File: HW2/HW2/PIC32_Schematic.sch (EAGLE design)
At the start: 22 parts

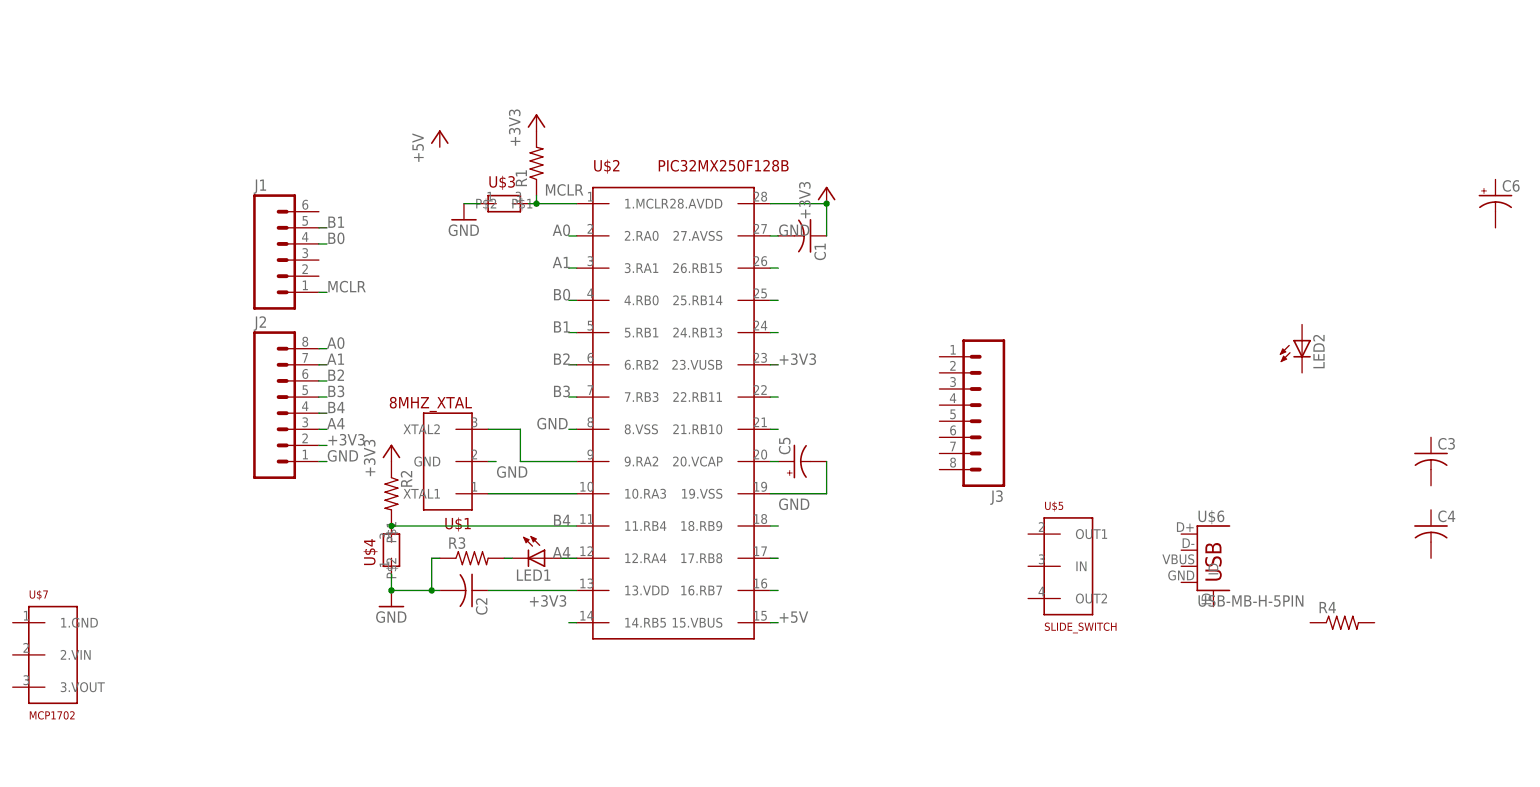
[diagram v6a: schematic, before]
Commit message: All PIC32 pins are now connected
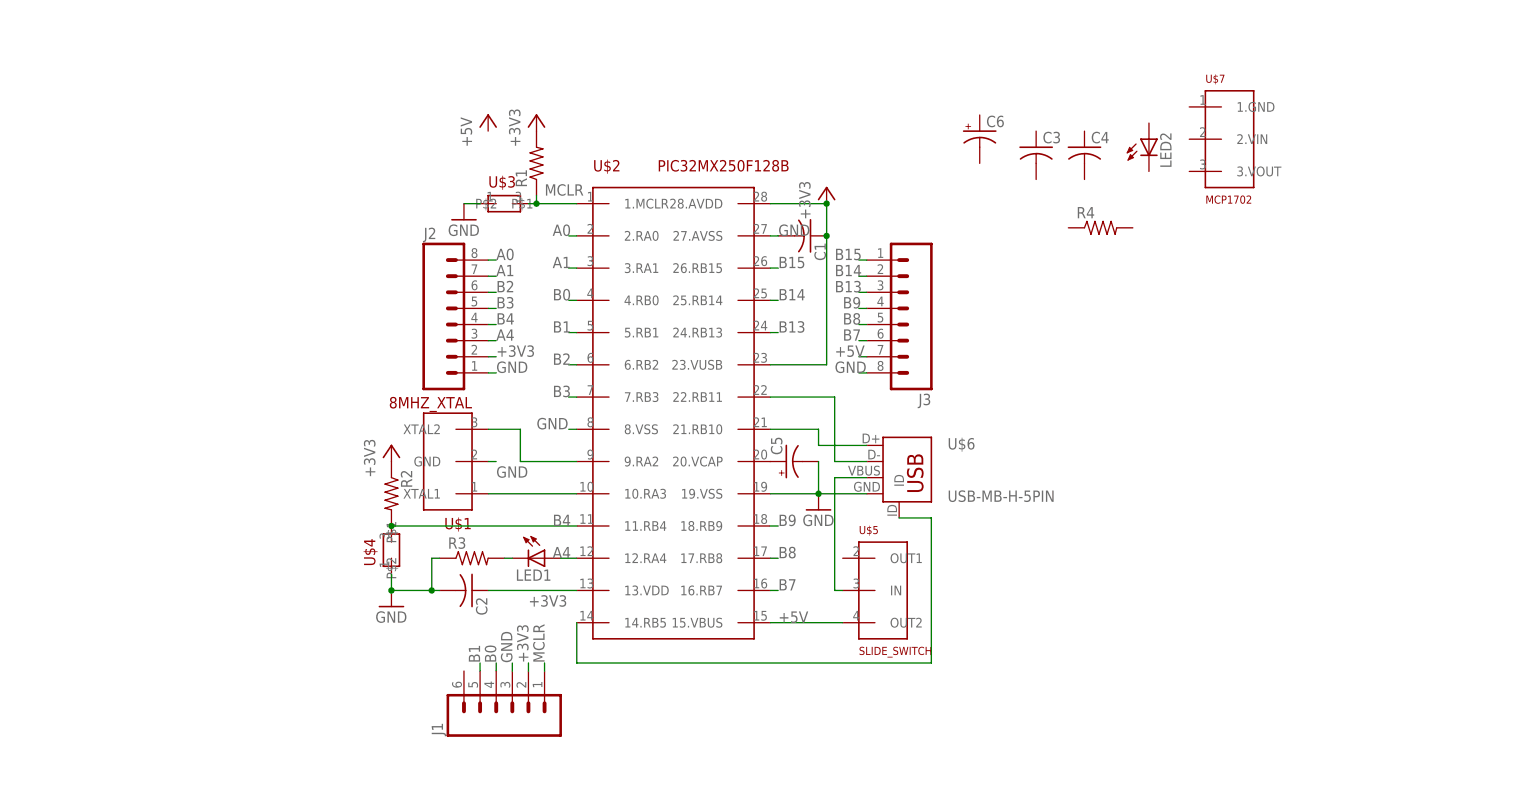
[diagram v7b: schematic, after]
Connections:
- removed net N$11: U$2.18.RB9
- removed net N$12: U$2.17.RB8
- removed net N$13: U$2.16.RB7
- removed net N$15: U$2.14.RB5
- removed net N$3: U$2.26.RB15
- removed net N$4: U$2.25.RB14
- removed net N$5: U$2.24.RB13
- removed net N$7: U$2.22.RB11
- removed net N$8: U$2.21.RB10
- new net B13: J3.3, U$2.24.RB13
- new net B14: J3.2, U$2.25.RB14
- new net B15: J3.1, U$2.26.RB15
- new net B7: J3.6, U$2.16.RB7
- new net B8: J3.5, U$2.17.RB8
- new net B9: J3.4, U$2.18.RB9
- new net D+: U$2.21.RB10, U$6.D+
- new net D-: U$2.22.RB11, U$6.D-
- new net ID: U$2.14.RB5, U$6.ID
- new net N$2: U$5.IN, U$6.VBUS
- net +3V3: now also J1.2
- net +5V: now also J3.7, U$5.OUT2
- net GND: now also J1.3, J3.8, U$6.GND
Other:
- moved on the sheet: C3, C4, C5, C6, J1, J2, J3, LED2, R4, U$5, U$7

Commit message: Schematic is complete; verification needed
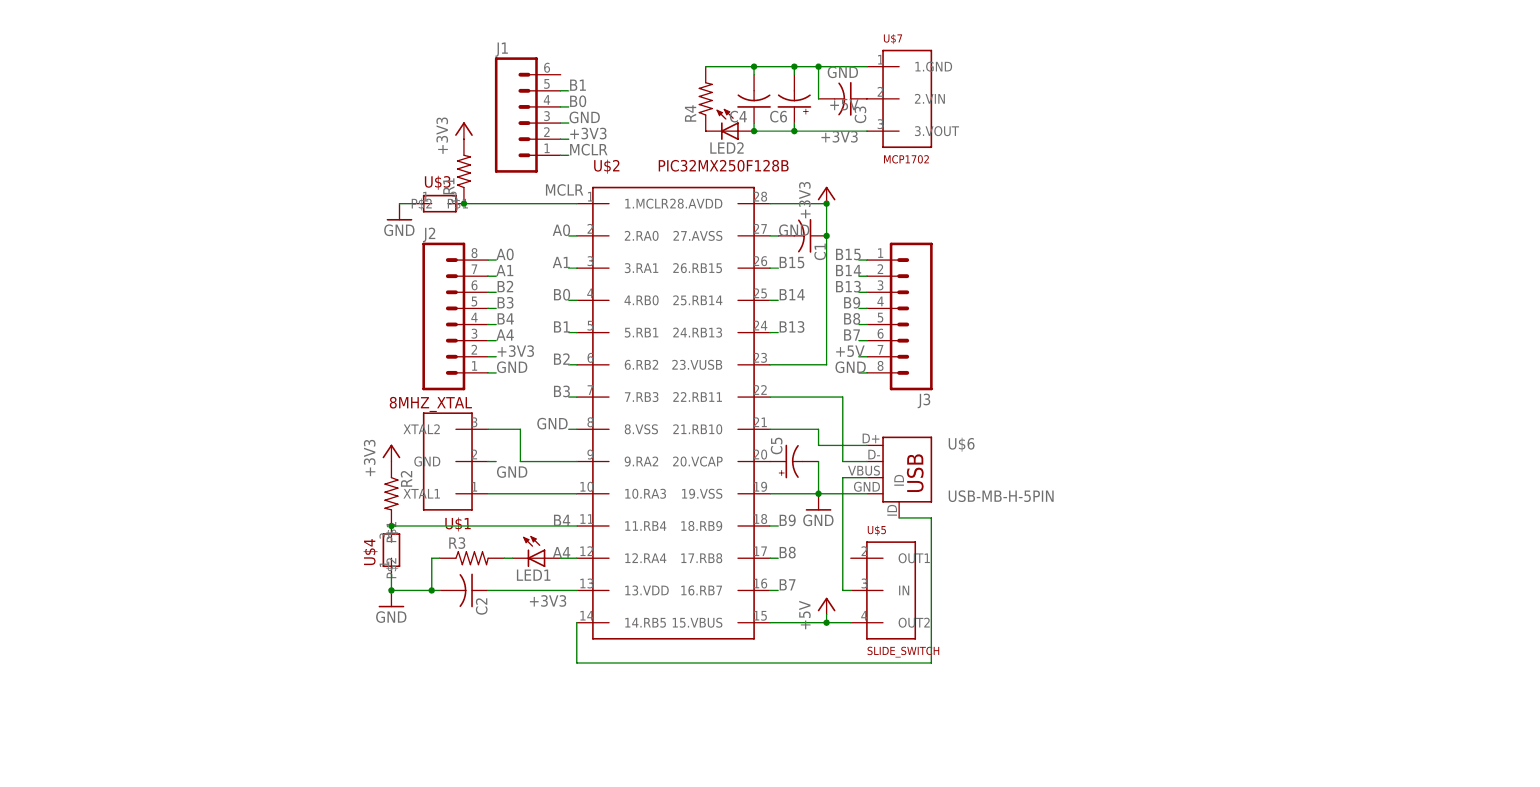
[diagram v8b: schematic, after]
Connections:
- new net N$3: LED2.C, R4.1
- net +3V3: now also C4.1, C6.+, LED2.A, U$7.3.VOUT
- net +5V: now also C3.1, U$7.2.VIN
- net GND: now also C3.2, C4.2, C6.-, R4.2, U$7.1.GND
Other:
- moved on the sheet: C3, C4, C6, J1, LED2, R1, R4, U$3, U$5, U$7
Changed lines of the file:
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@@
 <part name="R2" library="ME433" deviceset="R-US_" device="0207/10"/>
 <part name="R3" library="ME433" deviceset="R-US_" device="0207/10"/>
-<part name="R4" library="ME433" deviceset="R-US_" device="0207/10"/>
 <part name="C1" library="ME433" deviceset="C-US" device="025-024X044"/>
 <part name="C2" library="ME433" deviceset="C-US" device="025-024X044"/>
@@
 <part name="+3V3" library="ME433" deviceset="+3V3" device=""/>
 <part name="GND1" library="ME433" deviceset="GND" device=""/>
+<part name="R4" library="ME433" deviceset="R-US_" device="0207/10"/>
 </parts>
 <sheets>
@@
 <instance part="U$1" gate="G$1" x="-29.21" y="-2.54" rot="R180"/>
 <instance part="U$2" gate="G$1" x="0" y="0"/>
-<instance part="U$3" gate="G$1" x="-26.67" y="33.02"/>
+<instance part="U$3" gate="G$1" x="-36.83" y="33.02"/>
 <instance part="U$4" gate="G$1" x="-44.45" y="-21.59" rot="R90"/>
-<instance part="U$5" gate="G$1" x="34.29" y="-27.94"/>
+<instance part="U$5" gate="G$1" x="35.56" y="-27.94"/>
 <instance part="U$6" gate="G$1" x="35.56" y="-8.89"/>
-<instance part="U$7" gate="G$1" x="86.36" y="43.18"/>
-<instance part="J1" gate="G$1" x="-25.4" y="-45.72" rot="R90"/>
+<instance part="U$7" gate="G$1" x="35.56" y="49.53"/>
+<instance part="J1" gate="G$1" x="-22.86" y="45.72"/>
 <instance part="J2" gate="G$1" x="-34.29" y="13.97"/>
 <instance part="J3" gate="G$1" x="35.56" y="16.51" rot="R180"/>
 <instance part="LED1" gate="G$1" x="-20.32" y="-22.86" rot="R270"/>
-<instance part="LED2" gate="G$1" x="74.93" y="43.18"/>
-<instance part="R1" gate="G$1" x="-21.59" y="39.37" rot="R90"/>
+<instance part="LED2" gate="G$1" x="10.16" y="44.45" rot="R270"/>
+<instance part="R1" gate="G$1" x="-33.02" y="38.1" rot="R90"/>
 <instance part="R2" gate="G$1" x="-44.45" y="-12.7" rot="R270"/>
 <instance part="R3" gate="G$1" x="-31.75" y="-22.86"/>
-<instance part="R4" gate="G$1" x="67.31" y="29.21"/>
 <instance part="C1" gate="G$1" x="21.59" y="27.94" rot="R270"/>
 <instance part="C2" gate="G$1" x="-31.75" y="-27.94" rot="R270"/>
-<instance part="C3" gate="G$1" x="57.15" y="41.91"/>
-<instance part="C4" gate="G$1" x="64.77" y="41.91"/>
+<instance part="C3" gate="G$1" x="27.94" y="49.53" rot="R270"/>
+<instance part="C4" gate="G$1" x="12.7" y="48.26" rot="R180"/>
 <instance part="C5" gate="G$1" x="17.78" y="-7.62" rot="R90"/>
-<instance part="C6" gate="G$1" x="48.26" y="44.45"/>
+<instance part="C6" gate="G$1" x="19.05" y="48.26" rot="R180"/>
 <instance part="+3V1" gate="G$1" x="24.13" y="35.56"/>
-<instance part="P+1" gate="1" x="-29.21" y="46.99"/>
-<instance part="GND2" gate="1" x="-33.02" y="30.48"/>
-<instance part="+3V2" gate="G$1" x="-21.59" y="46.99"/>
+<instance part="P+1" gate="1" x="24.13" y="-29.21"/>
+<instance part="GND2" gate="1" x="-43.18" y="30.48"/>
+<instance part="+3V2" gate="G$1" x="-33.02" y="45.72"/>
 <instance part="GND3" gate="1" x="-44.45" y="-30.48"/>
 <instance part="+3V3" gate="G$1" x="-44.45" y="-5.08"/>
 <instance part="GND1" gate="1" x="22.86" y="-15.24"/>
+<instance part="R4" gate="G$1" x="5.08" y="49.53" rot="R90"/>
 </instances>
 <busses>
@@
 <segment>
 <pinref part="U$6" gate="G$1" pin="D-"/>
-<wire x1="25.4" y1="-7.62" x2="30.48" y2="-7.62" width="0.1524" layer="91"/>
+<wire x1="26.67" y1="-7.62" x2="30.48" y2="-7.62" width="0.1524" layer="91"/>
 <pinref part="U$2" gate="G$1" pin="22.RB11"/>
-<wire x1="15.24" y1="2.54" x2="25.4" y2="2.54" width="0.1524" layer="91"/>
-<wire x1="25.4" y1="2.54" x2="25.4" y2="-7.62" width="0.1524" layer="91"/>
+<wire x1="15.24" y1="2.54" x2="26.67" y2="2.54" width="0.1524" layer="91"/>
+<wire x1="26.67" y1="2.54" x2="26.67" y2="-7.62" width="0.1524" layer="91"/>
 </segment>
 </net>
@@
 <segment>
 <pinref part="U$2" gate="G$1" pin="15.VBUS"/>
-<label x="16.51" y="-33.02" size="1.778" layer="95"/>
 <pinref part="U$5" gate="G$1" pin="OUT2"/>
-<wire x1="15.24" y1="-33.02" x2="26.67" y2="-33.02" width="0.1524" layer="91"/>
+<wire x1="15.24" y1="-33.02" x2="24.13" y2="-33.02" width="0.1524" layer="91"/>
+<pinref part="P+1" gate="1" pin="+5V"/>
+<wire x1="24.13" y1="-33.02" x2="27.94" y2="-33.02" width="0.1524" layer="91"/>
+<wire x1="24.13" y1="-31.75" x2="24.13" y2="-33.02" width="0.1524" layer="91"/>
+<junction x="24.13" y="-33.02"/>
 </segment>
 <segment>
@@
 <label x="25.4" y="8.89" size="1.778" layer="95"/>
 </segment>
+<segment>
+<pinref part="U$7" gate="G$1" pin="2.VIN"/>
+<label x="29.21" y="49.53" size="1.778" layer="95" rot="R180"/>
+<pinref part="C3" gate="G$1" pin="1"/>
+</segment>
 </net>
 <net name="N$19" class="0">
@@
 <segment>
 <pinref part="U$2" gate="G$1" pin="1.MCLR"/>
-<wire x1="-15.24" y1="33.02" x2="-21.59" y2="33.02" width="0.1524" layer="91"/>
+<wire x1="-15.24" y1="33.02" x2="-33.02" y2="33.02" width="0.1524" layer="91"/>
 <pinref part="U$3" gate="G$1" pin="P$2"/>
 <label x="-20.32" y="34.29" size="1.778" layer="95"/>
-<wire x1="-21.59" y1="33.02" x2="-22.86" y2="33.02" width="0.1524" layer="91"/>
-<wire x1="-21.59" y1="33.02" x2="-21.59" y2="34.29" width="0.1524" layer="91"/>
-<junction x="-21.59" y="33.02"/>
+<junction x="-33.02" y="33.02"/>
 <pinref part="R1" gate="G$1" pin="1"/>
 </segment>
 <segment>
 <pinref part="J1" gate="G$1" pin="1"/>
-<wire x1="-20.32" y1="-40.64" x2="-20.32" y2="-39.37" width="0.1524" layer="91"/>
-<label x="-20.32" y="-39.37" size="1.778" layer="95" rot="R90"/>
+<wire x1="-17.78" y1="40.64" x2="-16.51" y2="40.64" width="0.1524" layer="91"/>
+<label x="-16.51" y="40.64" size="1.778" layer="95"/>
 </segment>
 </net>
@@
 <segment>
 <pinref part="J1" gate="G$1" pin="2"/>
-<wire x1="-22.86" y1="-40.64" x2="-22.86" y2="-39.37" width="0.1524" layer="91"/>
-<label x="-22.86" y="-39.37" size="1.778" layer="95" rot="R90"/>
+<wire x1="-17.78" y1="43.18" x2="-16.51" y2="43.18" width="0.1524" layer="91"/>
+<label x="-16.51" y="43.18" size="1.778" layer="95"/>
+</segment>
+<segment>
+<pinref part="U$7" gate="G$1" pin="3.VOUT"/>
+<wire x1="30.48" y1="44.45" x2="19.05" y2="44.45" width="0.1524" layer="91"/>
+<label x="29.21" y="44.45" size="1.778" layer="95" rot="R180"/>
+<pinref part="LED2" gate="G$1" pin="A"/>
+<pinref part="C6" gate="G$1" pin="+"/>
+<wire x1="19.05" y1="44.45" x2="12.7" y2="44.45" width="0.1524" layer="91"/>
+<wire x1="19.05" y1="45.72" x2="19.05" y2="44.45" width="0.1524" layer="91"/>
+<junction x="19.05" y="44.45"/>
+<pinref part="C4" gate="G$1" pin="1"/>
+<wire x1="12.7" y1="45.72" x2="12.7" y2="44.45" width="0.1524" layer="91"/>
+<junction x="12.7" y="44.45"/>
 </segment>
 </net>
@@
 <segment>
 <pinref part="U$3" gate="G$1" pin="P$1"/>
-<wire x1="-30.48" y1="33.02" x2="-33.02" y2="33.02" width="0.1524" layer="91"/>
+<wire x1="-40.64" y1="33.02" x2="-43.18" y2="33.02" width="0.1524" layer="91"/>
 <pinref part="GND2" gate="1" pin="GND"/>
 </segment>
@@
 <segment>
 <pinref part="J1" gate="G$1" pin="3"/>
-<wire x1="-25.4" y1="-40.64" x2="-25.4" y2="-39.37" width="0.1524" layer="91"/>
-<label x="-25.4" y="-39.37" size="1.778" layer="95" rot="R90"/>
+<wire x1="-17.78" y1="45.72" x2="-16.51" y2="45.72" width="0.1524" layer="91"/>
+<label x="-16.51" y="45.72" size="1.778" layer="95"/>
 </segment>
 <segment>
@@
 <wire x1="30.48" y1="6.35" x2="29.21" y2="6.35" width="0.1524" layer="91"/>
 <label x="25.4" y="6.35" size="1.778" layer="95"/>
+</segment>
+<segment>
+<pinref part="U$7" gate="G$1" pin="1.GND"/>
+<label x="29.21" y="54.61" size="1.778" layer="95" rot="R180"/>
+<wire x1="30.48" y1="54.61" x2="22.86" y2="54.61" width="0.1524" layer="91"/>
+<pinref part="R4" gate="G$1" pin="2"/>
+<wire x1="22.86" y1="54.61" x2="19.05" y2="54.61" width="0.1524" layer="91"/>
+<wire x1="19.05" y1="54.61" x2="12.7" y2="54.61" width="0.1524" layer="91"/>
+<wire x1="12.7" y1="54.61" x2="5.08" y2="54.61" width="0.1524" layer="91"/>
+<pinref part="C4" gate="G$1" pin="2"/>
+<wire x1="12.7" y1="53.34" x2="12.7" y2="54.61" width="0.1524" layer="91"/>
+<junction x="12.7" y="54.61"/>
+<pinref part="C6" gate="G$1" pin="-"/>
+<wire x1="19.05" y1="53.34" x2="19.05" y2="54.61" width="0.1524" layer="91"/>
+<junction x="19.05" y="54.61"/>
+<pinref part="C3" gate="G$1" pin="2"/>
+<wire x1="22.86" y1="49.53" x2="22.86" y2="54.61" width="0.1524" layer="91"/>
+<junction x="22.86" y="54.61"/>
 </segment>
 </net>
@@
 <segment>
 <pinref part="J1" gate="G$1" pin="4"/>
-<wire x1="-27.94" y1="-40.64" x2="-27.94" y2="-39.37" width="0.1524" layer="91"/>
-<label x="-27.94" y="-39.37" size="1.778" layer="95" rot="R90"/>
+<wire x1="-17.78" y1="48.26" x2="-16.51" y2="48.26" width="0.1524" layer="91"/>
+<label x="-16.51" y="48.26" size="1.778" layer="95"/>
 </segment>
 <segment>
@@
 <segment>
 <pinref part="J1" gate="G$1" pin="5"/>
-<wire x1="-30.48" y1="-40.64" x2="-30.48" y2="-39.37" width="0.1524" layer="91"/>
-<label x="-30.48" y="-39.37" size="1.778" layer="95" rot="R90"/>
+<wire x1="-17.78" y1="50.8" x2="-16.51" y2="50.8" width="0.1524" layer="91"/>
+<label x="-16.51" y="50.8" size="1.778" layer="95"/>
 </segment>
 <segment>
@@
 <segment>
 <pinref part="U$5" gate="G$1" pin="IN"/>
-<wire x1="26.67" y1="-27.94" x2="25.4" y2="-27.94" width="0.1524" layer="91"/>
-<wire x1="25.4" y1="-27.94" x2="25.4" y2="-10.16" width="0.1524" layer="91"/>
+<wire x1="27.94" y1="-27.94" x2="26.67" y2="-27.94" width="0.1524" layer="91"/>
+<wire x1="26.67" y1="-27.94" x2="26.67" y2="-10.16" width="0.1524" layer="91"/>
 <pinref part="U$6" gate="G$1" pin="VBUS"/>
-<wire x1="25.4" y1="-10.16" x2="30.48" y2="-10.16" width="0.1524" layer="91"/>
+<wire x1="26.67" y1="-10.16" x2="30.48" y2="-10.16" width="0.1524" layer="91"/>
 </segment>
 </net>
@@
 </segment>
 </net>
+<net name="N$3" class="0">
+<segment>
+<pinref part="LED2" gate="G$1" pin="C"/>
+<pinref part="R4" gate="G$1" pin="1"/>
+</segment>
+</net>
